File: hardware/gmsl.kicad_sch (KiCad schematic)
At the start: 28 parts, among them Q1 DMG1012T, Q2 DMG1012T, U1 MAX96717GTJ/VY+

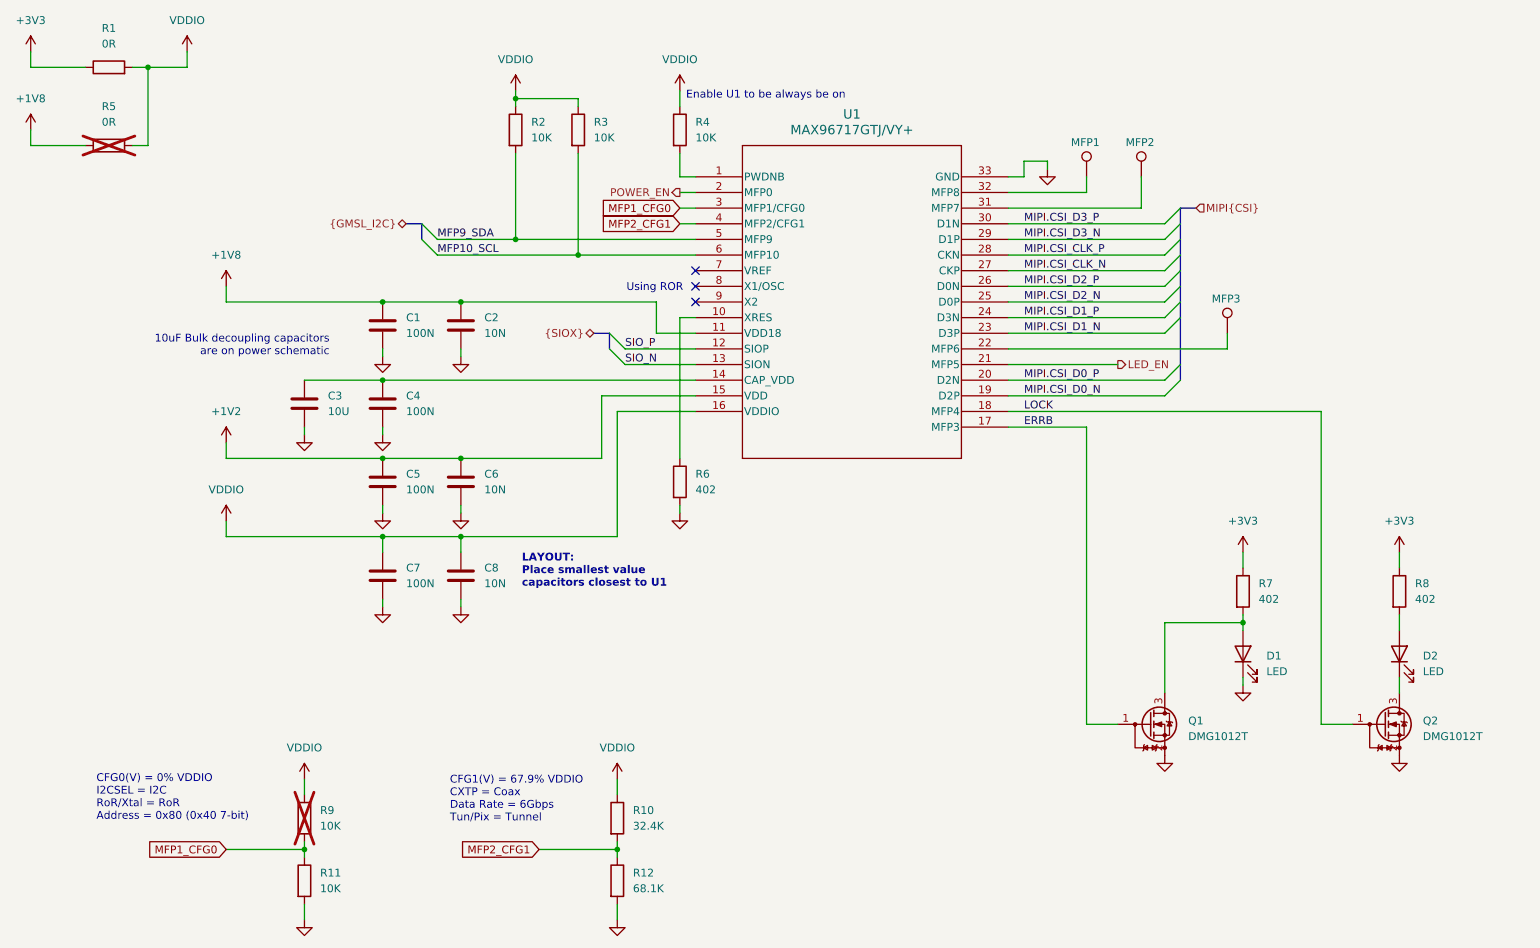
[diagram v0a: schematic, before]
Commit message: cleaned up fakra footprint
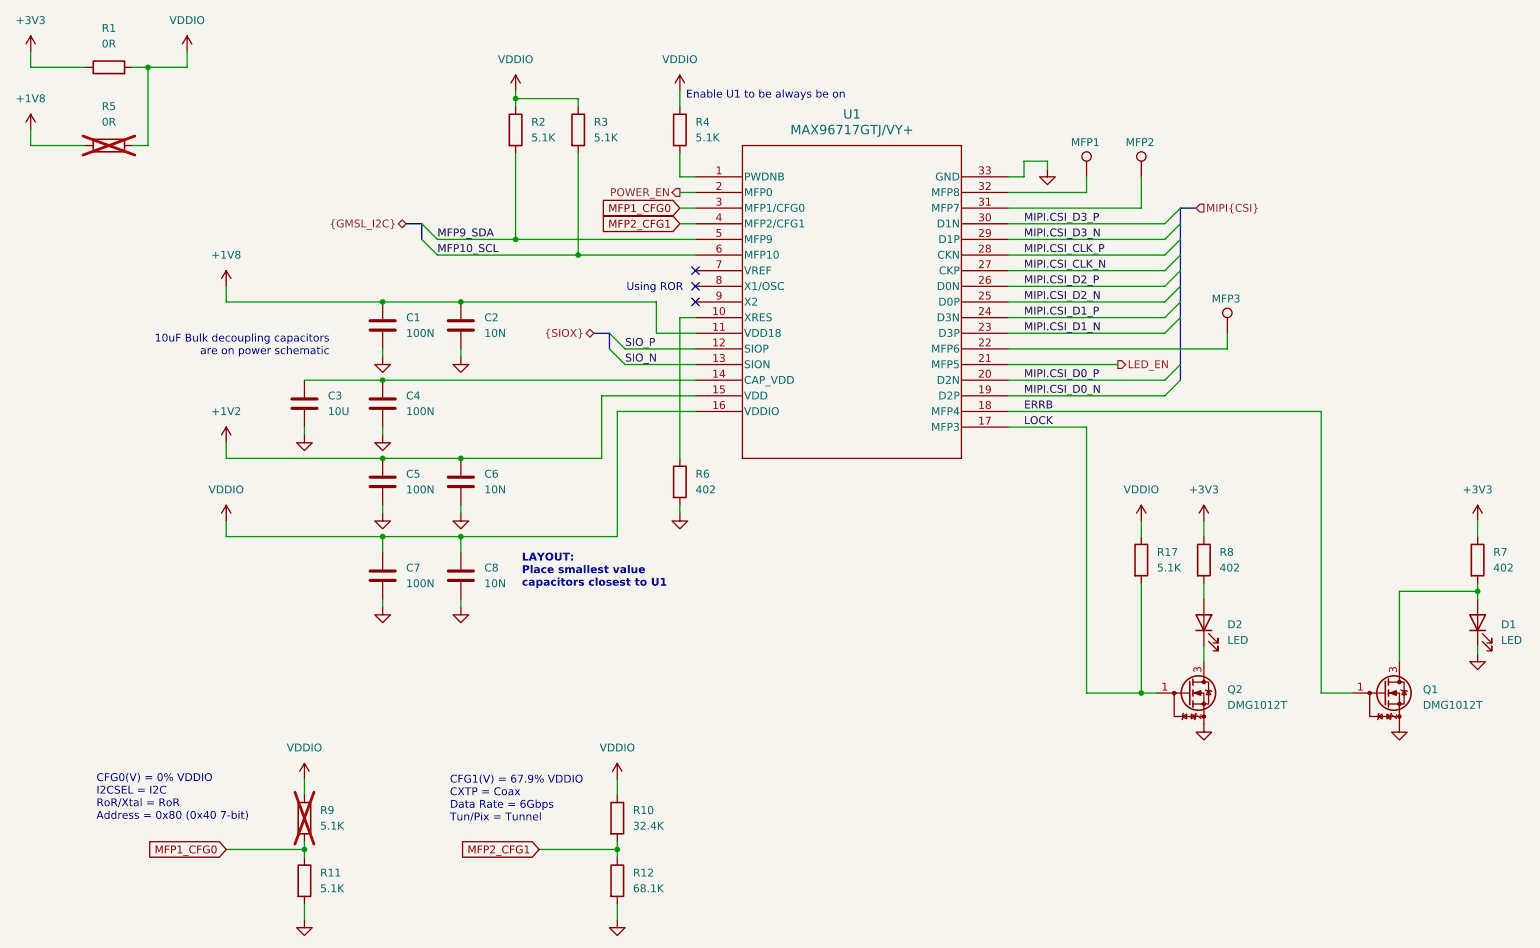
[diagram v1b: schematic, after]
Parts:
- added R17: 5.1K, Resistor_SMD:R_0402_1005Metric, symbol Device:R
- R11, R2, R3, R4, R9: value 10K -> 5.1K
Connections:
- net ERRB: now also U1.18 (MFP4); no longer U1.17 (MFP3)
- net LOCK: now also U1.17 (MFP3), R17.2; no longer U1.18 (MFP4)
- net VDDIO: now also R17.1
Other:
- moved on the sheet: D1, D2, Q1, Q2, R7, R8

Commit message: finished schematics and layout, need final aesthetic touches
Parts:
- added R18: 5.1K, Resistor_SMD:R_0402_1005Metric, symbol Device:R
- C3: footprint Capacitor_SMD:C_0402_1005Metric -> Capacitor_SMD:C_0603_1608Metric
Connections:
- net ERRB: now also R18.2
- net VDDIO: now also R18.1
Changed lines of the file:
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@@
 	)
 	(junction
+		(at 245.11 139.7)
+		(diameter 0)
+		(color 0 0 0 0)
+	)
+	(junction
 		(at 88.9 88.9)
 		(diameter 0)
@@
 	(wire
 		(pts
+			(xy 245.11 113.03) (xy 245.11 116.84)
+		)
+		(stroke
+			(width 0)
+			(type default)
+		)
+	)
+	(wire
+		(pts
 			(xy 266.7 123.19) (xy 266.7 124.46)
 		)
@@
 	(wire
 		(pts
-			(xy 190.5 93.98) (xy 241.3 93.98)
+			(xy 190.5 93.98) (xy 236.22 93.98)
 		)
 		(stroke
@@
 	(wire
 		(pts
+			(xy 245.11 139.7) (xy 246.38 139.7)
+		)
+		(stroke
+			(width 0)
+			(type default)
+		)
+	)
+	(wire
+		(pts
 			(xy 190.5 88.9) (xy 215.9 88.9)
 		)
@@
 	(wire
 		(pts
-			(xy 241.3 93.98) (xy 241.3 139.7)
+			(xy 236.22 93.98) (xy 236.22 139.7)
 		)
 		(stroke
@@
 	(wire
 		(pts
+			(xy 245.11 124.46) (xy 245.11 139.7)
+		)
+		(stroke
+			(width 0)
+			(type default)
+		)
+	)
+	(wire
+		(pts
 			(xy 137.16 63.5) (xy 139.7 63.5)
 		)
@@
 	(wire
 		(pts
-			(xy 241.3 139.7) (xy 246.38 139.7)
+			(xy 236.22 139.7) (xy 245.11 139.7)
 		)
 		(stroke
@@
 	)
 	(symbol
+		(lib_id "power:VDD")
+		(at 245.11 113.03 0)
+		(unit 1)
+		(exclude_from_sim no)
+		(in_bom yes)
+		(on_board yes)
+		(dnp no)
+		(fields_autoplaced yes)
+		(property "Reference" "#PWR053"
+			(at 245.11 116.84 0)
+			(effects
+				(font
+					(size 1.27 1.27)
+				)
+				(hide yes)
+			)
+		)
+		(property "Value" "VDDIO"
+			(at 245.11 107.95 0)
+			(effects
+				(font
+					(size 1.27 1.27)
+				)
+			)
+		)
+		(property "Footprint" ""
+			(at 245.11 113.03 0)
+			(effects
+				(font
+					(size 1.27 1.27)
+				)
+				(hide yes)
+			)
+		)
+		(property "Datasheet" ""
+			(at 245.11 113.03 0)
+			(effects
+				(font
+					(size 1.27 1.27)
+				)
+				(hide yes)
+			)
+		)
+		(property "Description" "Power symbol creates a global label with name \"VDD\""
+			(at 245.11 113.03 0)
+			(effects
+				(font
+					(size 1.27 1.27)
+				)
+				(hide yes)
+			)
+		)
+		(pin "1"
+		)
+		(instances
+			(project "minimax"
+				(path "/d9b03904-3e0d-40cc-bc70-bbd63756773a/7d5b9018-1d5d-4fe7-9ecf-86a5900c7cec"
+					(reference "#PWR053")
+					(unit 1)
+				)
+			)
+		)
+	)
+	(symbol
 		(lib_id "Device:R")
 		(at 127 170.18 0)
@@
 	(symbol
 		(lib_id "Device:C")
-		(at 76.2 92.71 0)
-		(unit 1)
-		(exclude_from_sim no)
-		(in_bom yes)
-		(on_board yes)
-		(dnp no)
-		(fields_autoplaced yes)
-		(property "Reference" "C3"
-			(at 80.01 91.4399 0)
-			(effects
-				(font
-					(size 1.27 1.27)
-				)
-				(justify left)
-			)
-		)
-		(property "Value" "10U"
-			(at 80.01 93.9799 0)
-			(effects
-				(font
-					(size 1.27 1.27)
-				)
-				(justify left)
-			)
-		)
-		(property "Footprint" "Capacitor_SMD:C_0402_1005Metric"
-			(at 77.1652 96.52 0)
-			(effects
-				(font
-					(size 1.27 1.27)
-				)
-				(hide yes)
-			)
-		)
-		(property "Datasheet" "~"
-			(at 76.2 92.71 0)
-			(effects
-				(font
-					(size 1.27 1.27)
-				)
-				(hide yes)
-			)
-		)
-		(property "Description" "Unpolarized capacitor"
-			(at 76.2 92.71 0)
-			(effects
-				(font
-					(size 1.27 1.27)
-				)
-				(hide yes)
-			)
-		)
-		(pin "2"
-		)
-		(pin "1"
-		)
-		(instances
-			(project "minimax"
-				(path "/d9b03904-3e0d-40cc-bc70-bbd63756773a/7d5b9018-1d5d-4fe7-9ecf-86a5900c7cec"
-					(reference "C3")
-					(unit 1)
-				)
-			)
-		)
-	)
-	(symbol
-		(lib_id "Device:C")
 		(at 101.6 120.65 0)
 		(unit 1)
@@
 	)
 	(symbol
+		(lib_id "Device:R")
+		(at 245.11 120.65 0)
+		(unit 1)
+		(exclude_from_sim no)
+		(in_bom yes)
+		(on_board yes)
+		(dnp no)
+		(fields_autoplaced yes)
+		(property "Reference" "R18"
+			(at 247.65 119.3799 0)
+			(effects
+				(font
+					(size 1.27 1.27)
+				)
+				(justify left)
+			)
+		)
+		(property "Value" "5.1K"
+			(at 247.65 121.9199 0)
+			(effects
+				(font
+					(size 1.27 1.27)
+				)
+				(justify left)
+			)
+		)
+		(property "Footprint" "Resistor_SMD:R_0402_1005Metric"
+			(at 243.332 120.65 90)
+			(effects
+				(font
+					(size 1.27 1.27)
+				)
+				(hide yes)
+			)
+		)
+		(property "Datasheet" "~"
+			(at 245.11 120.65 0)
+			(effects
+				(font
+					(size 1.27 1.27)
+				)
+				(hide yes)
+			)
+		)
+		(property "Description" "Resistor"
+			(at 245.11 120.65 0)
+			(effects
+				(font
+					(size 1.27 1.27)
+				)
+				(hide yes)
+			)
+		)
+		(pin "2"
+		)
+		(pin "1"
+		)
+		(instances
+			(project "minimax"
+				(path "/d9b03904-3e0d-40cc-bc70-bbd63756773a/7d5b9018-1d5d-4fe7-9ecf-86a5900c7cec"
+					(reference "R18")
+					(unit 1)
+				)
+			)
+		)
+	)
+	(symbol
 		(lib_id "power:GND")
 		(at 76.2 176.53 0)
@@
 					(unit 1)
 				)
+			)
+		)
+	)
+	(symbol
+		(lib_id "Device:C")
+		(at 76.2 92.71 0)
+		(unit 1)
+		(exclude_from_sim no)
+		(in_bom yes)
+		(on_board yes)
+		(dnp no)
+		(fields_autoplaced yes)
+		(property "Reference" "C3"
+			(at 80.01 91.4399 0)
+			(effects
+				(font
+					(size 1.27 1.27)
+				)
+				(justify left)
+			)
+		)
+		(property "Value" "10U"
+			(at 80.01 93.9799 0)
+			(effects
+				(font
+					(size 1.27 1.27)
+				)
+				(justify left)
+			)
+		)
+		(property "Footprint" "Capacitor_SMD:C_0603_1608Metric"
+			(at 77.1652 96.52 0)
+			(effects
+				(font
+					(size 1.27 1.27)
+				)
+				(hide yes)
+			)
+		)
+		(property "Datasheet" "~"
+			(at 76.2 92.71 0)
+			(effects
+				(font
+					(size 1.27 1.27)
+				)
+				(hide yes)
+			)
+		)
+		(property "Description" "Unpolarized capacitor"
+			(at 76.2 92.71 0)
+			(effects
+				(font
+					(size 1.27 1.27)
+				)
+				(hide yes)
+			)
+		)
+		(pin "1"
+		)
+		(pin "2"
+		)
+		(instances
+			(project "minimax"
+				(path "/d9b03904-3e0d-40cc-bc70-bbd63756773a/7d5b9018-1d5d-4fe7-9ecf-86a5900c7cec"
+					(reference "C3")
+					(unit 1)
+				)

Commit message: submitted for board fab
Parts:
- renumbered MFP3 to MFP6, MFP2 to MFP7, MFP1 to MFP8, R4 to R17, R6 to R18, R17 to R4, R18 to R6
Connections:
- net ERRB: now also Q2.1 (G); no longer Q1.1 (G)
- net LOCK: now also Q1.1 (G); no longer Q2.1 (G)
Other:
- moved on the sheet: R4, R6

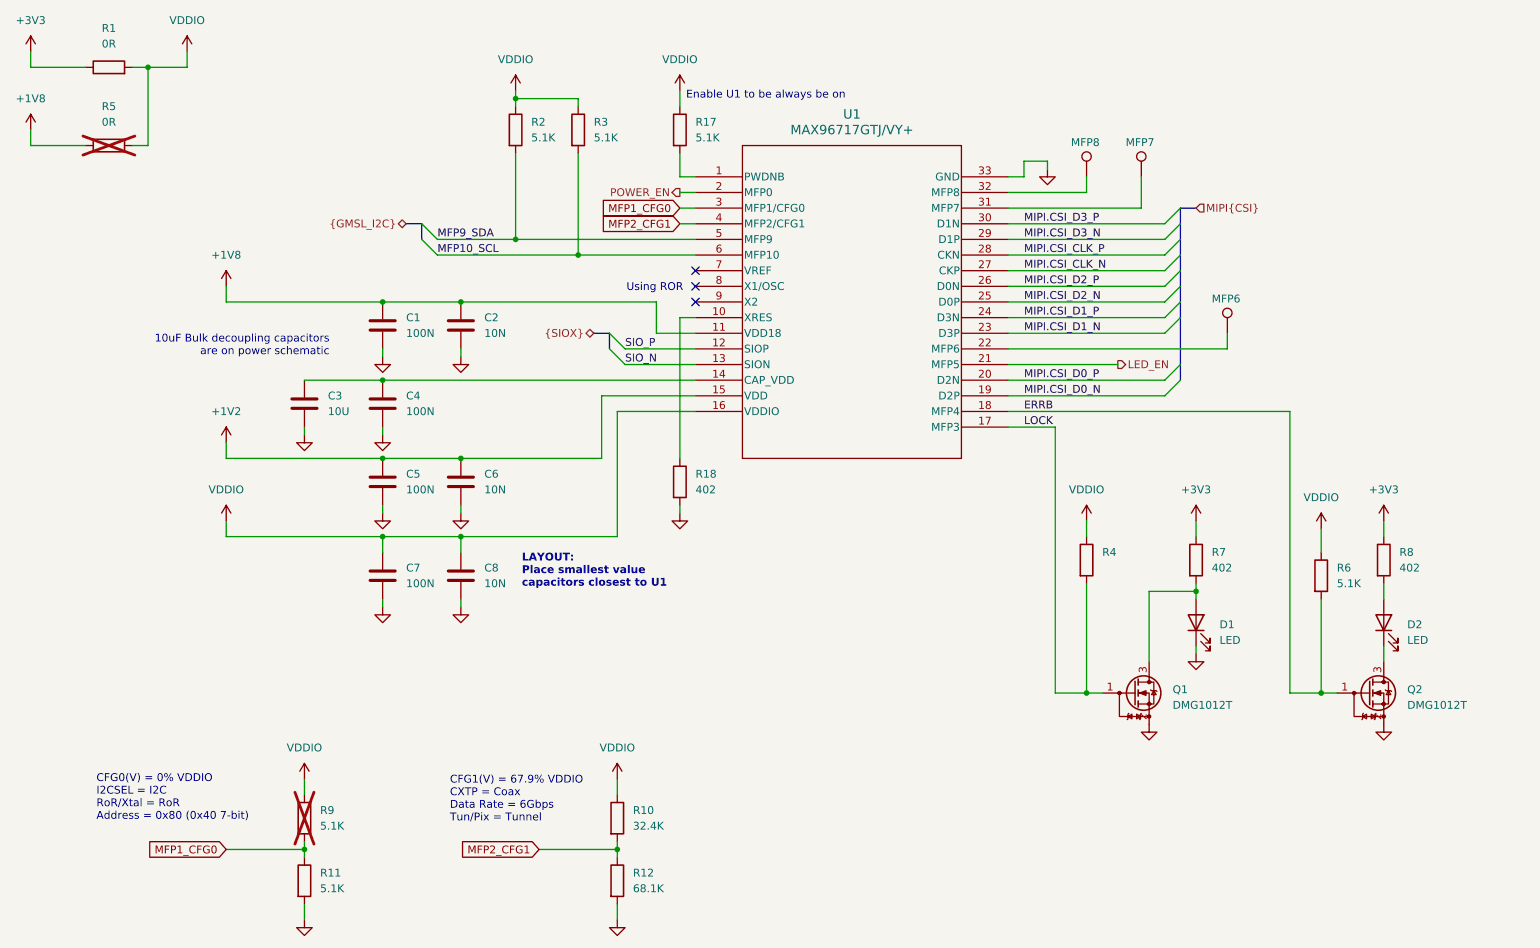
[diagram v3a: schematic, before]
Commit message: fixed LED logic and added pullup on the camera enable
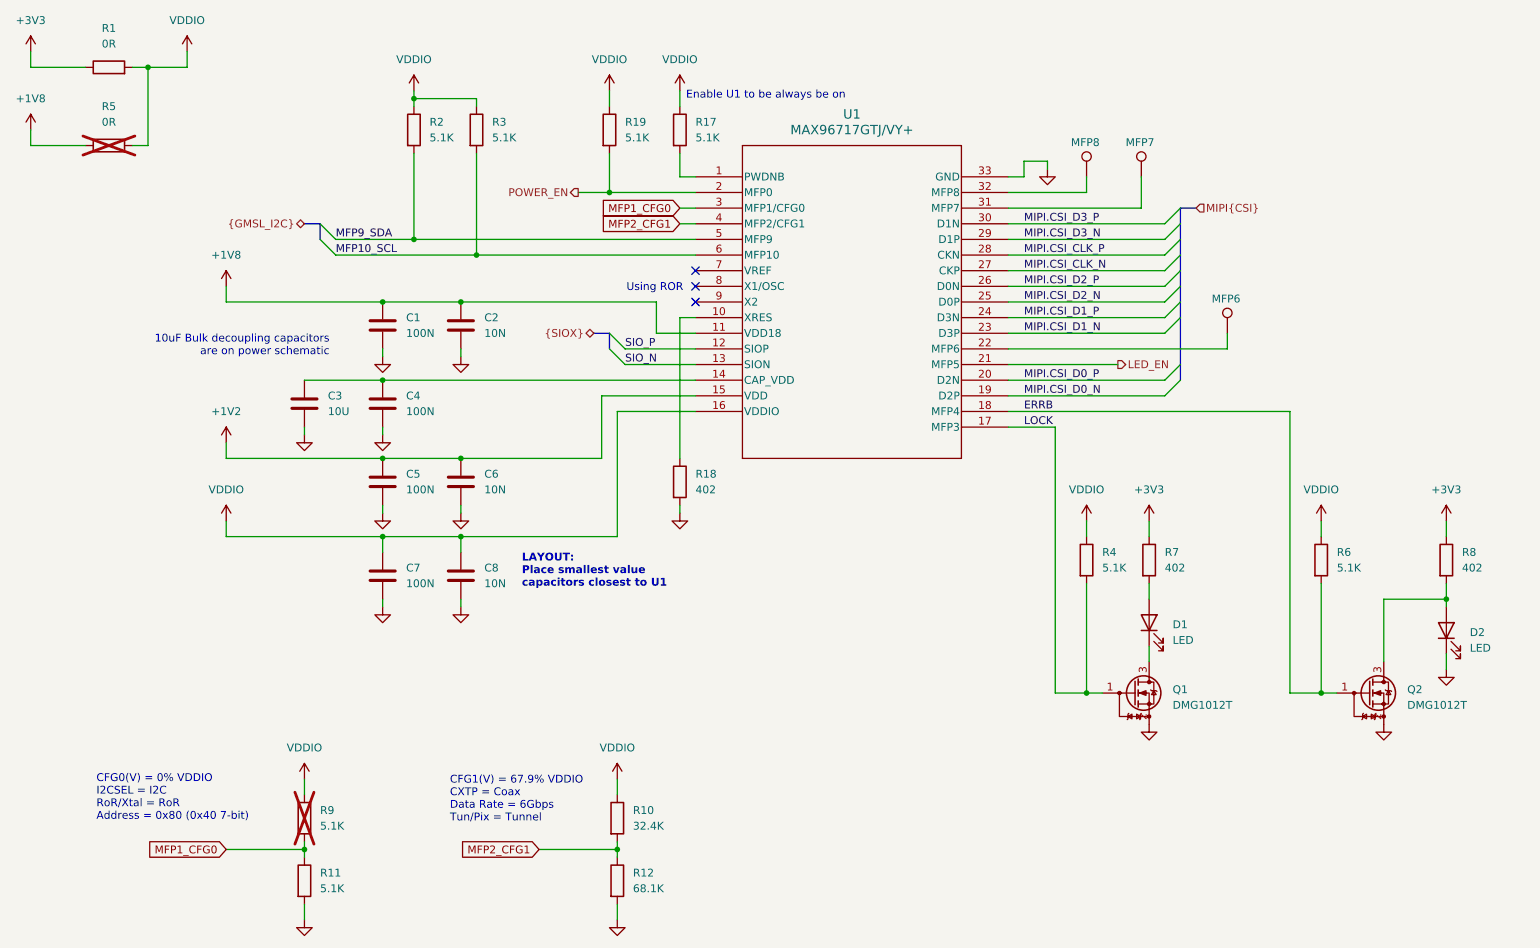
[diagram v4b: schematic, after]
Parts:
- added R19: 5.1K, Resistor_SMD:R_0402_1005Metric, symbol Device:R
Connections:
- net GND: now also D2.1 (K); no longer D1.1 (K)
- net POWER_EN: now also R19.2
- net VDDIO: now also R19.1
- net at D1.2 (A), R7.2: no longer Q1.3 (D)
- net at D2.2 (A), R8.2: now also Q2.3 (D)
- new net: D1.1 (K), Q1.3 (D)
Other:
- moved on the sheet: D1, D2, R2, R3, R6, R7, R8

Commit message: prepping for fab
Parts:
- removed MFP6, MFP7, MFP8: TestPoint, Connector_Pin:Pin_D1.0mm_L10.0mm, symbol Connector:TestPoint
- added TP1: MFP8, TestPoint:TestPoint_THTPad_D1.0mm_Drill0.5mm, symbol Connector:TestPoint
- added TP2: MFP7, TestPoint:TestPoint_THTPad_D1.0mm_Drill0.5mm, symbol Connector:TestPoint
- added TP3: MFP6, TestPoint:TestPoint_THTPad_D1.0mm_Drill0.5mm, symbol Connector:TestPoint
- R9: value 5.1K -> 5.1k
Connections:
- net at U1.31 (MFP7): now also TP2.1
- net at U1.22 (MFP6): now also TP3.1
- net at U1.32 (MFP8): now also TP1.1
